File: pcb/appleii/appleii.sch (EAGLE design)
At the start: 30 parts, among them J1 ATX24RH

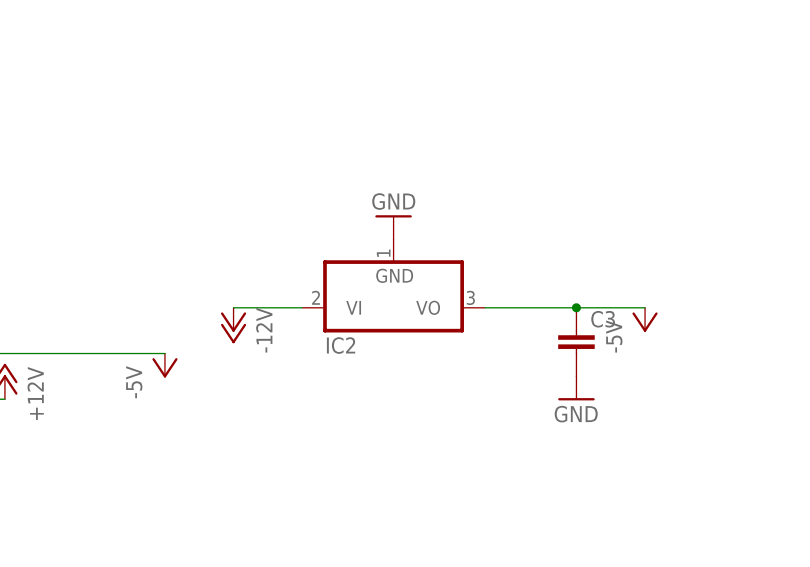
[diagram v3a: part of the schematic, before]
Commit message: switched back to 7905
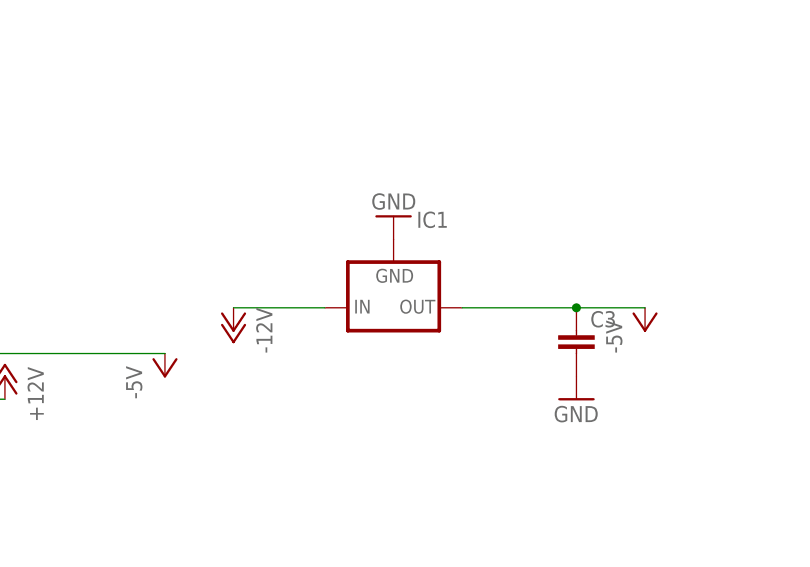
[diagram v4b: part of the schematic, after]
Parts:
- removed IC2: (no value), linear:7905L
- added IC1: (no value), v-reg:79XXS
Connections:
- net -12V: now also IC1.IN; no longer IC2.VI
- net -5V: now also IC1.OUT; no longer IC2.VO
- net GND: now also IC1.GND; no longer IC2.GND
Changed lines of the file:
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@@
 <part name="C9" library="capacitor-wima" library_urn="urn:adsk.eagle:library:116" deviceset="C" device="5/2.5" package3d_urn="urn:adsk.eagle:package:5426/1"/>
 <part name="GND25" library="supply1" library_urn="urn:adsk.eagle:library:371" deviceset="GND" device=""/>
-<part name="IC2" library="linear" library_urn="urn:adsk.eagle:library:262" deviceset="79*" device="L" package3d_urn="urn:adsk.eagle:package:16416/2" technology="05"/>
 <part name="C1" library="adafruit" deviceset="CPOL-US" device="E5-10.5"/>
 <part name="GND9" library="supply1" library_urn="urn:adsk.eagle:library:371" deviceset="GND" device=""/>
 <part name="C4" library="adafruit" deviceset="CPOL-US" device="E5-10.5"/>
 <part name="C5" library="capacitor-wima" library_urn="urn:adsk.eagle:library:116" deviceset="C" device="5/2.5" package3d_urn="urn:adsk.eagle:package:5426/1"/>
+<part name="IC1" library="v-reg" library_urn="urn:adsk.eagle:library:409" deviceset="79XXS" device="" package3d_urn="urn:adsk.eagle:package:30343/1"/>
 </parts>
 <sheets>
@@
 <attribute name="VALUE" x="190.5" y="162.56" size="1.778" layer="96"/>
 </instance>
-<instance part="IC2" gate="A1" x="152.4" y="99.06" smashed="yes">
-<attribute name="NAME" x="144.78" y="91.44" size="1.778" layer="95"/>
-<attribute name="VALUE" x="144.78" y="88.9" size="1.778" layer="96"/>
-</instance>
 <instance part="C1" gate="G$1" x="144.78" y="193.04" smashed="yes">
 <attribute name="NAME" x="145.796" y="193.675" size="1.778" layer="95"/>
@@
 <attribute name="NAME" x="169.164" y="193.421" size="1.778" layer="95"/>
 <attribute name="VALUE" x="169.164" y="188.341" size="1.778" layer="96"/>
+</instance>
+<instance part="IC1" gate="1" x="152.4" y="96.52" smashed="yes">
+<attribute name="NAME" x="154.94" y="105.41" size="1.778" layer="95"/>
+<attribute name="VALUE" x="154.94" y="102.87" size="1.778" layer="96"/>
 </instance>
 </instances>
@@
 </segment>
 <segment>
-<pinref part="IC2" gate="A1" pin="GND"/>
-<pinref part="GND5" gate="1" pin="GND"/>
-</segment>
-<segment>
 <pinref part="C1" gate="G$1" pin="-"/>
 <wire x1="144.78" y1="187.96" x2="149.86" y2="187.96" width="0.1524" layer="91"/>
@@
 <wire x1="149.86" y1="187.96" x2="167.64" y2="187.96" width="0.1524" layer="91"/>
 </segment>
+<segment>
+<pinref part="IC1" gate="1" pin="GND"/>
+<pinref part="GND5" gate="1" pin="GND"/>
+</segment>
 </net>
 <net name="-12V" class="0">
@@
 <segment>
 <pinref part="P-3" gate="1" pin="-12V"/>
-<pinref part="IC2" gate="A1" pin="VI"/>
-<wire x1="134.62" y1="96.52" x2="142.24" y2="96.52" width="0.1524" layer="91"/>
+<wire x1="134.62" y1="96.52" x2="144.78" y2="96.52" width="0.1524" layer="91"/>
+<pinref part="IC1" gate="1" pin="IN"/>
 </segment>
 </net>
@@
 <wire x1="172.72" y1="96.52" x2="180.34" y2="96.52" width="0.1524" layer="91"/>
 <junction x="172.72" y="96.52"/>
-<pinref part="IC2" gate="A1" pin="VO"/>
-<wire x1="162.56" y1="96.52" x2="172.72" y2="96.52" width="0.1524" layer="91"/>
-</segment>
-<segment>
+<wire x1="160.02" y1="96.52" x2="172.72" y2="96.52" width="0.1524" layer="91"/>
+<pinref part="IC1" gate="1" pin="OUT"/>
+</segment>
+<segment>

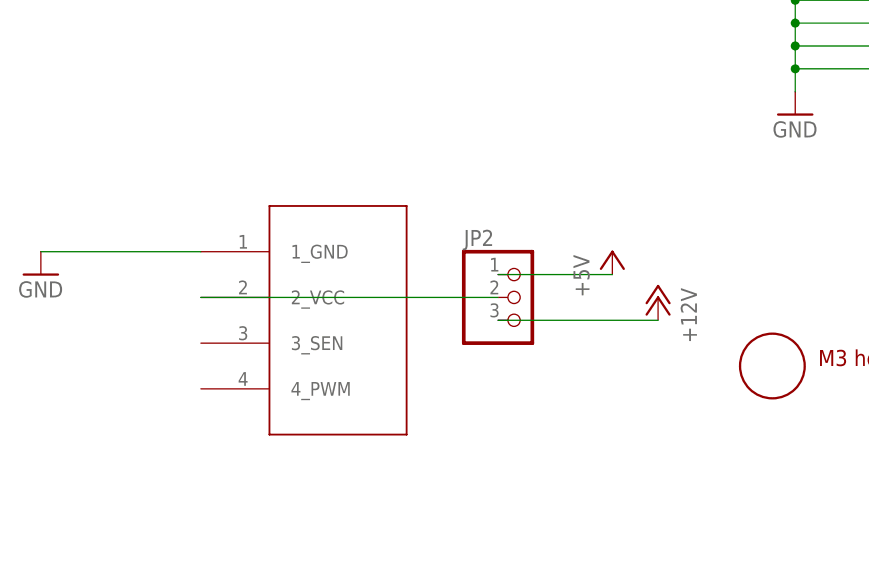
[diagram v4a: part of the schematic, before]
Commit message: added more caps
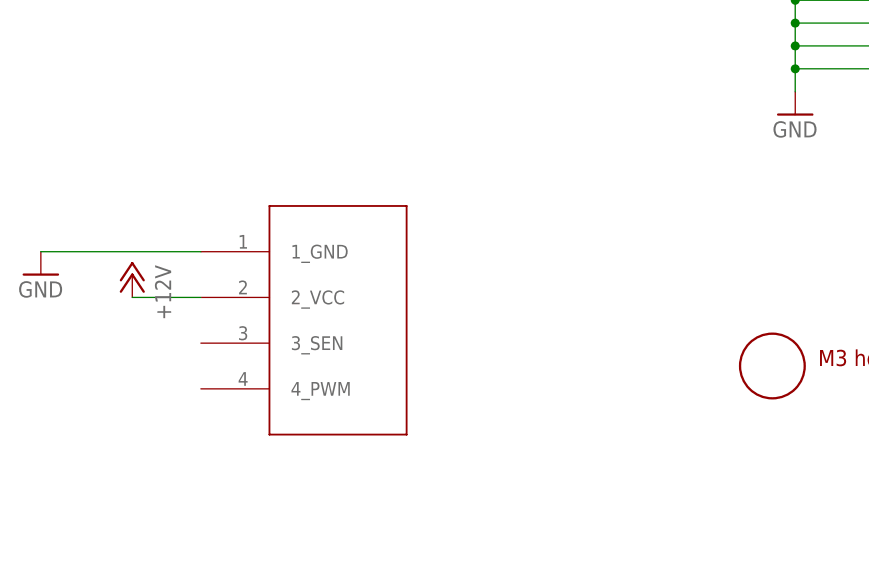
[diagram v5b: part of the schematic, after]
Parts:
- removed JP2: (no value), pinhead:PINHD-1X3
- C1, C4: device adafruit:CPOL-USE5-10.5 -> adafruit_changed:CPOL-USE3.5-8
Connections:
- removed net N$1: JP2.2, JP3.2_VCC
- net +12V: now also JP3.2_VCC; no longer JP2.3
- net +5V: no longer JP2.1
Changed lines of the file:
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@@
 <part name="P+5" library="supply1" library_urn="urn:adsk.eagle:library:371" deviceset="+12V" device=""/>
 <part name="GND7" library="supply1" library_urn="urn:adsk.eagle:library:371" deviceset="GND" device=""/>
-<part name="P+9" library="supply1" library_urn="urn:adsk.eagle:library:371" deviceset="+5V" device=""/>
 <part name="J1" library="macse" deviceset="ATX24" device="RH"/>
 <part name="U$5" library="a" deviceset="M3_MOUNTING_HOLE" device=""/>
@@
 <part name="GND11" library="supply1" library_urn="urn:adsk.eagle:library:371" deviceset="GND" device=""/>
 <part name="JP3" library="appleii" deviceset="4PIN_FAN" device=""/>
-<part name="JP2" library="pinhead" library_urn="urn:adsk.eagle:library:325" deviceset="PINHD-1X3" device="" package3d_urn="urn:adsk.eagle:package:22458/2"/>
 <part name="U$7" library="atx4vc" deviceset="EDGEPAD" device=""/>
 <part name="GND4" library="supply1" library_urn="urn:adsk.eagle:library:371" deviceset="GND" device=""/>
@@
 <part name="C9" library="capacitor-wima" library_urn="urn:adsk.eagle:library:116" deviceset="C" device="5/2.5" package3d_urn="urn:adsk.eagle:package:5426/1"/>
 <part name="GND25" library="supply1" library_urn="urn:adsk.eagle:library:371" deviceset="GND" device=""/>
-<part name="C1" library="adafruit" deviceset="CPOL-US" device="E5-10.5"/>
+<part name="C1" library="adafruit_changed" deviceset="CPOL-US" device="E3.5-8"/>
 <part name="GND9" library="supply1" library_urn="urn:adsk.eagle:library:371" deviceset="GND" device=""/>
-<part name="C4" library="adafruit" deviceset="CPOL-US" device="E5-10.5"/>
+<part name="C4" library="adafruit_changed" deviceset="CPOL-US" device="E3.5-8"/>
 <part name="C5" library="capacitor-wima" library_urn="urn:adsk.eagle:library:116" deviceset="C" device="5/2.5" package3d_urn="urn:adsk.eagle:package:5426/1"/>
 <part name="IC1" library="v-reg" library_urn="urn:adsk.eagle:library:409" deviceset="79XXS" device="" package3d_urn="urn:adsk.eagle:package:30343/1"/>
@@
 <attribute name="VALUE" x="147.32" y="154.94" size="1.778" layer="96"/>
 </instance>
-<instance part="P+5" gate="1" x="53.34" y="129.54" smashed="yes" rot="MR0">
-<attribute name="VALUE" x="55.88" y="124.46" size="1.778" layer="96" rot="MR90"/>
+<instance part="P+5" gate="1" x="-5.08" y="132.08" smashed="yes" rot="MR0">
+<attribute name="VALUE" x="-2.54" y="127" size="1.778" layer="96" rot="MR90"/>
 </instance>
 <instance part="GND7" gate="1" x="-15.24" y="132.08" smashed="yes">
 <attribute name="VALUE" x="-17.78" y="129.54" size="1.778" layer="96"/>
-</instance>
-<instance part="P+9" gate="1" x="48.26" y="134.62" smashed="yes">
-<attribute name="VALUE" x="45.72" y="129.54" size="1.778" layer="96" rot="R90"/>
 </instance>
 <instance part="J1" gate="G$1" x="96.52" y="175.26" smashed="yes">
@@
 </instance>
 <instance part="JP3" gate="A" x="15.24" y="127" smashed="yes"/>
-<instance part="JP2" gate="A" x="38.1" y="129.54" smashed="yes">
-<attribute name="NAME" x="31.75" y="135.255" size="1.778" layer="95"/>
-<attribute name="VALUE" x="31.75" y="121.92" size="1.778" layer="96"/>
-</instance>
 <instance part="U$7" gate="G$1" x="-2.54" y="71.12" smashed="yes"/>
 <instance part="GND4" gate="1" x="-12.7" y="68.58" smashed="yes">
@@
 <wire x1="73.66" y1="86.36" x2="78.74" y2="86.36" width="0.1524" layer="91"/>
 </segment>
-<segment>
-<pinref part="JP2" gate="A" pin="1"/>
-<pinref part="P+9" gate="1" pin="+5V"/>
-<wire x1="35.56" y1="132.08" x2="48.26" y2="132.08" width="0.1524" layer="91"/>
-</segment>
 </net>
 <net name="N$8" class="0">
@@
 <segment>
 <pinref part="P+5" gate="1" pin="+12V"/>
-<pinref part="JP2" gate="A" pin="3"/>
-<wire x1="53.34" y1="127" x2="35.56" y2="127" width="0.1524" layer="91"/>
+<pinref part="JP3" gate="A" pin="2_VCC"/>
+<wire x1="-5.08" y1="129.54" x2="2.54" y2="129.54" width="0.1524" layer="91"/>
 </segment>
 </net>
@@
 </segment>
 </net>
-<net name="N$1" class="0">
-<segment>
-<pinref part="JP2" gate="A" pin="2"/>
-<pinref part="JP3" gate="A" pin="2_VCC"/>
-<wire x1="35.56" y1="129.54" x2="2.54" y2="129.54" width="0.1524" layer="91"/>
-</segment>
-</net>

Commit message: cleanup for new run
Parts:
- added C2: (no value), capacitor-wima:C5/2.5
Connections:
- net +12V: now also C5.1
- net +5V: now also C2.1
- net GND: now also C2.2
- net N$8: no longer C5.1
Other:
- moved on the sheet: C5
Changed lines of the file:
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@@
 <part name="C5" library="capacitor-wima" library_urn="urn:adsk.eagle:library:116" deviceset="C" device="5/2.5" package3d_urn="urn:adsk.eagle:package:5426/1"/>
 <part name="IC1" library="v-reg" library_urn="urn:adsk.eagle:library:409" deviceset="79XXS" device="" package3d_urn="urn:adsk.eagle:package:30343/1"/>
+<part name="GND10" library="supply1" library_urn="urn:adsk.eagle:library:371" deviceset="GND" device=""/>
+<part name="C2" library="capacitor-wima" library_urn="urn:adsk.eagle:library:116" deviceset="C" device="5/2.5" package3d_urn="urn:adsk.eagle:package:5426/1"/>
 </parts>
 <sheets>
@@
 <attribute name="VALUE" x="6.096" y="173.609" size="1.778" layer="96"/>
 </instance>
-<instance part="C5" gate="G$1" x="167.64" y="193.04" smashed="yes">
-<attribute name="NAME" x="169.164" y="193.421" size="1.778" layer="95"/>
-<attribute name="VALUE" x="169.164" y="188.341" size="1.778" layer="96"/>
+<instance part="C5" gate="G$1" x="200.66" y="172.72" smashed="yes">
+<attribute name="NAME" x="202.184" y="173.101" size="1.778" layer="95"/>
+<attribute name="VALUE" x="202.184" y="168.021" size="1.778" layer="96"/>
 </instance>
 <instance part="IC1" gate="1" x="152.4" y="96.52" smashed="yes">
 <attribute name="NAME" x="154.94" y="105.41" size="1.778" layer="95"/>
 <attribute name="VALUE" x="154.94" y="102.87" size="1.778" layer="96"/>
+</instance>
+<instance part="GND10" gate="1" x="200.66" y="165.1" smashed="yes">
+<attribute name="VALUE" x="198.12" y="162.56" size="1.778" layer="96"/>
+</instance>
+<instance part="C2" gate="G$1" x="27.94" y="177.8" smashed="yes">
+<attribute name="NAME" x="29.464" y="178.181" size="1.778" layer="95"/>
+<attribute name="VALUE" x="29.464" y="173.101" size="1.778" layer="96"/>
 </instance>
 </instances>
@@
 <pinref part="C4" gate="G$1" pin="-"/>
 <wire x1="12.7" y1="172.72" x2="5.08" y2="172.72" width="0.1524" layer="91"/>
+<pinref part="C2" gate="G$1" pin="2"/>
+<wire x1="27.94" y1="172.72" x2="20.32" y2="172.72" width="0.1524" layer="91"/>
+<junction x="20.32" y="172.72"/>
 </segment>
 <segment>
@@
 <wire x1="144.78" y1="187.96" x2="149.86" y2="187.96" width="0.1524" layer="91"/>
 <pinref part="GND9" gate="1" pin="GND"/>
-<junction x="149.86" y="187.96"/>
-<pinref part="C5" gate="G$1" pin="2"/>
-<wire x1="149.86" y1="187.96" x2="167.64" y2="187.96" width="0.1524" layer="91"/>
 </segment>
 <segment>
 <pinref part="IC1" gate="1" pin="GND"/>
 <pinref part="GND5" gate="1" pin="GND"/>
+</segment>
+<segment>
+<pinref part="C5" gate="G$1" pin="2"/>
+<pinref part="GND10" gate="1" pin="GND"/>
 </segment>
 </net>
@@
 <pinref part="C4" gate="G$1" pin="+"/>
 <wire x1="12.7" y1="180.34" x2="5.08" y2="180.34" width="0.1524" layer="91"/>
+<pinref part="C2" gate="G$1" pin="1"/>
+<wire x1="20.32" y1="180.34" x2="27.94" y2="180.34" width="0.1524" layer="91"/>
+<junction x="20.32" y="180.34"/>
 </segment>
 <segment>
@@
 <pinref part="J1" gate="G$1" pin="12V@1"/>
 <pinref part="C1" gate="G$1" pin="+"/>
-<wire x1="144.78" y1="195.58" x2="167.64" y2="195.58" width="0.1524" layer="91"/>
 <wire x1="139.954" y1="173.99" x2="139.954" y2="195.58" width="0.1524" layer="91"/>
 <wire x1="139.954" y1="195.58" x2="144.78" y2="195.58" width="0.1524" layer="91"/>
 <junction x="139.954" y="173.99"/>
-<junction x="144.78" y="195.58"/>
-<pinref part="C5" gate="G$1" pin="1"/>
 </segment>
 </net>
@@
 <wire x1="193.04" y1="177.8" x2="180.34" y2="177.8" width="0.1524" layer="91"/>
 <junction x="180.34" y="177.8"/>
-</segment>
-<segment>
+<pinref part="C5" gate="G$1" pin="1"/>
+<wire x1="193.04" y1="177.8" x2="200.66" y2="177.8" width="0.1524" layer="91"/>
+<wire x1="200.66" y1="177.8" x2="200.66" y2="175.26" width="0.1524" layer="91"/>
+<junction x="193.04" y="177.8"/>
+</segment>
+<segment>
